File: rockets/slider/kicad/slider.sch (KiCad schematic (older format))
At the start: 34 parts

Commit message: More shematic
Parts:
- added J?: SWD Breakout, symbol Connector:Conn_01x03_Male
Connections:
- net Buzzer_EN: now also U?.19 (GPIO14)
- net GND: now also J?.2 (Pin_2)
- net PWM_Buzzer: now also U?.17 (GPIO13)
- net SWD_CLK: now reaches U?.41 (SWCLK)
- net SWD_CLK: now also J?.3 (Pin_3)
- net SWD_IO: now reaches U?.43 (SWDIO)
- net SWD_IO: now also J?.1 (Pin_1)
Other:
- moved on the sheet: BT?, BZ?, C?, D?, J?, LS?, M?, Q?, R?, SW?, U?

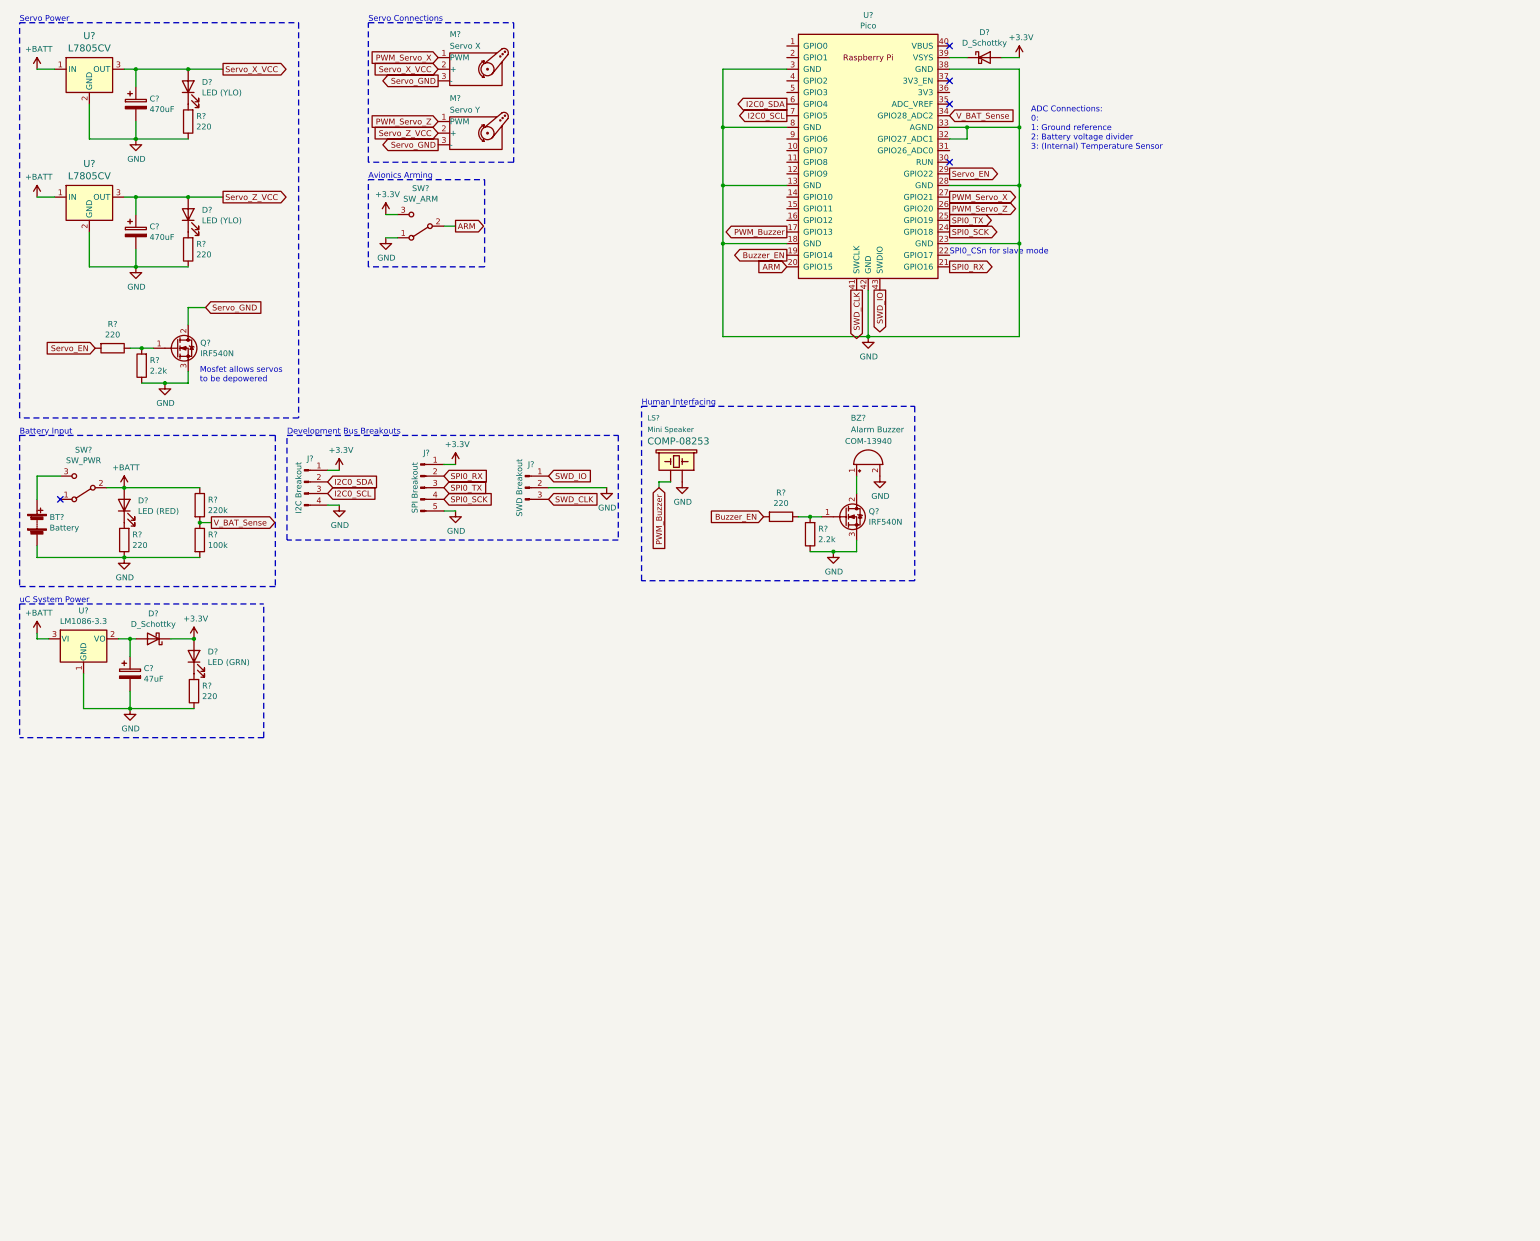
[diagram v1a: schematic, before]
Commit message: Change schematic layout
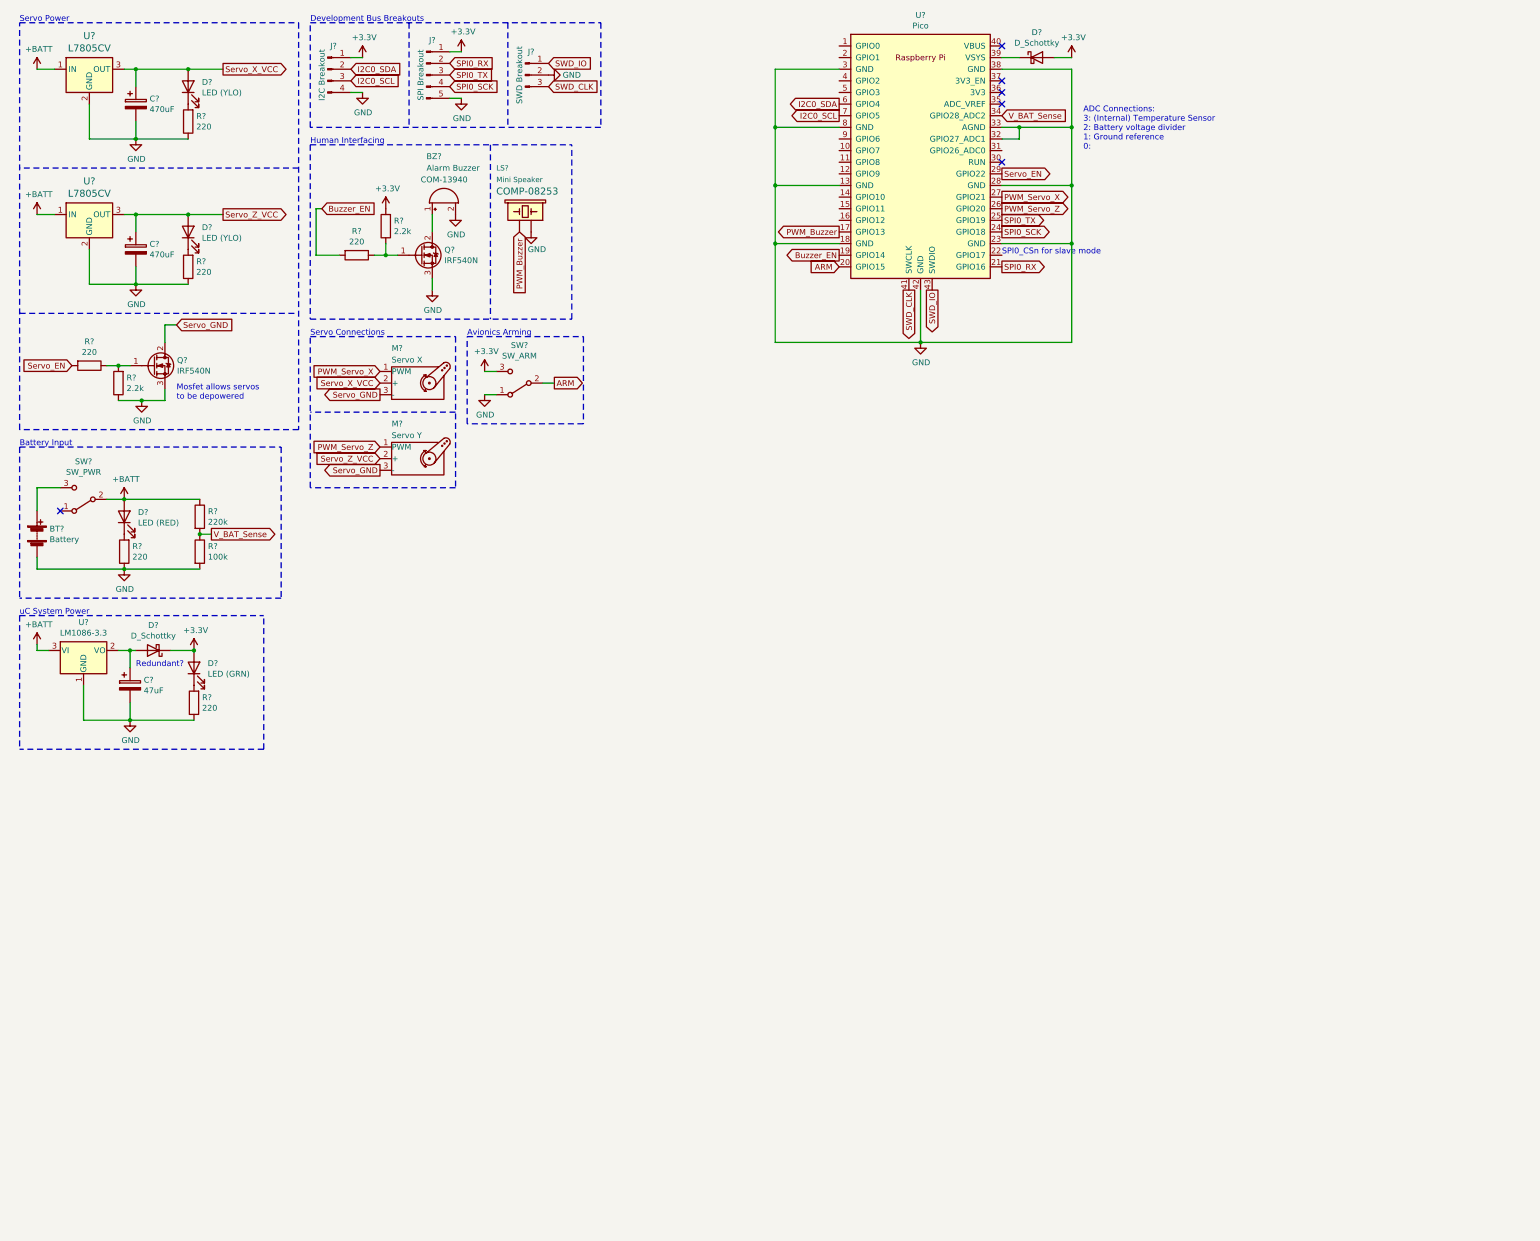
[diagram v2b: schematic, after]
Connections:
- net +3V3: now also R?.2
- net GND: no longer R?.1
- net at Q?.1 (G), R?.1: now also R?.1; no longer R?.2
- no-connect marks 5 -> 6
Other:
- note added: "ADC Connections:\n3: (Internal) Temperature Sensor\n2: Battery voltage divider\n1: Ground reference\n0:"
- note added: "Redundant?"
- note removed: "ADC Connections:\n0:\n1: Ground reference\n2: Battery voltage divider\n3: (Internal) Temperature Sensor"
- moved on the sheet: BT?, BZ?, C?, D?, J?, LS?, M?, Q?, R?, SW?, U?

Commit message: layouting
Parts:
- removed D?: D_Schottky, symbol Device:D_Schottky
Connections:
- net +3V3: now also C?.1, U?.2 (VO)
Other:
- note added: "L7805CV\nMin: +2v = 7v\nMax: 35v"
- note added: "LM1086-3.3\nMin: +1.5v = 4.8v\nMax: +27v = 30.3v"
- note added: "Min: 7v (L785CV)\nMax: 30.3v (LM1086-3.3)"
- note removed: "Redundant?"
- moved on the sheet: BT?, C?, D?, R?, SW?, U?

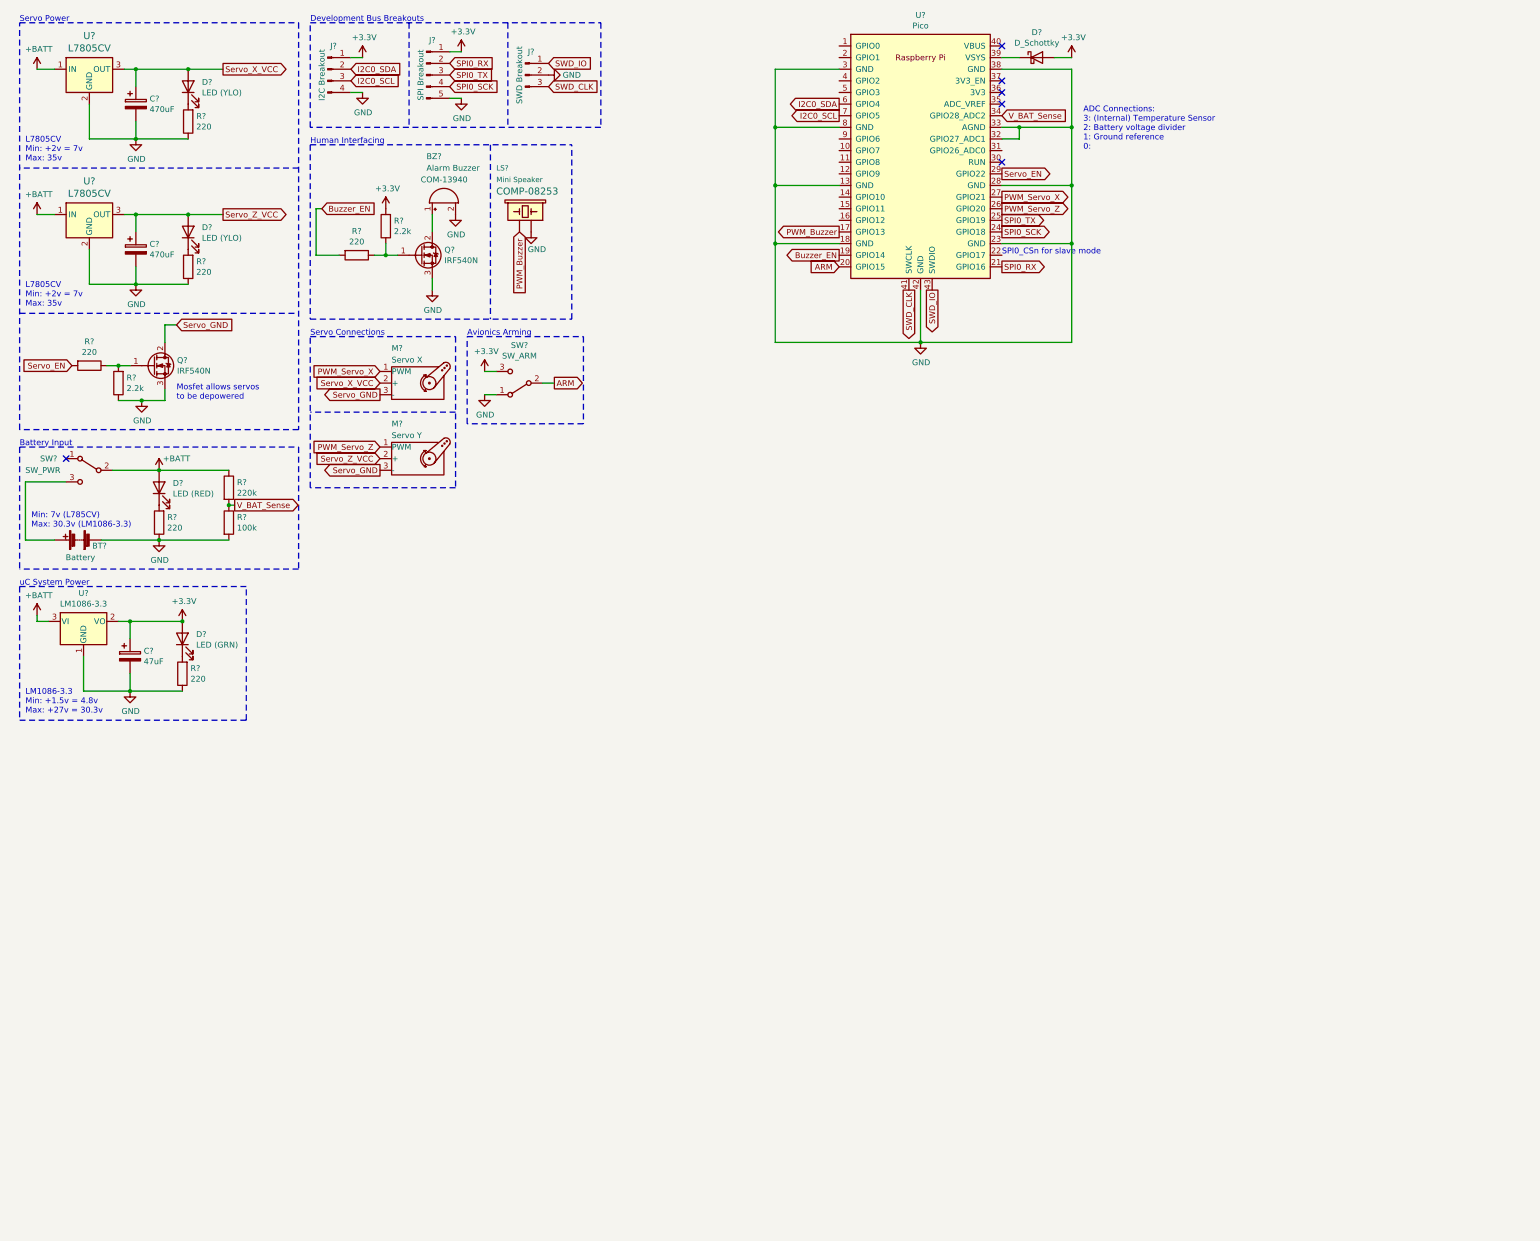
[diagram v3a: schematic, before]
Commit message: assigned footprints
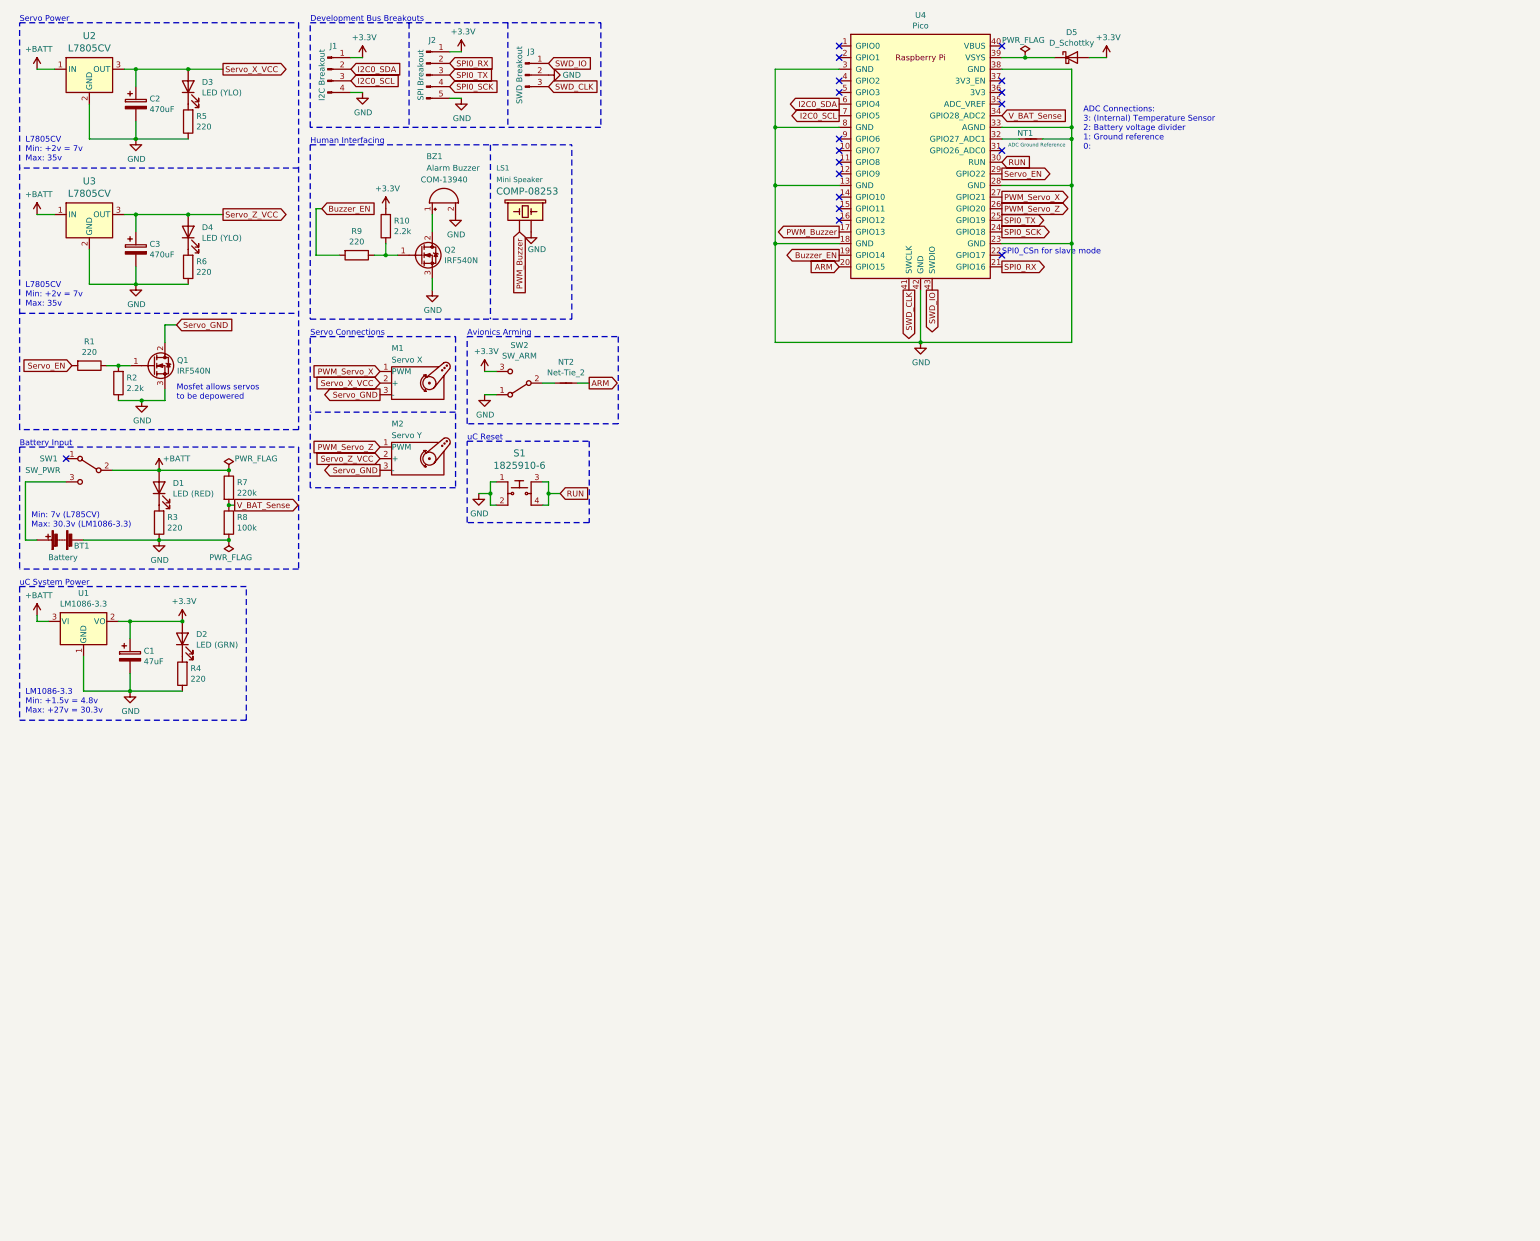
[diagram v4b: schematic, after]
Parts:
- added NT1: ADC Ground Reference, NetTie:NetTie-2_SMD_Pad2.0mm, symbol Device:Net-Tie_2
- added NT2: Net-Tie_2, NetTie:NetTie-2_SMD_Pad2.0mm, symbol Device:Net-Tie_2
- added S1: 1825910-6, digikey-footprints:Switch_Tactile_THT_6x6mm, symbol dk_Tactile-Switches:1825910-6
- D1, D2, D3, D4: renamed from D?; footprint (none) -> LED_THT:LED_D5.0mm
- D5: renamed from D?; footprint (none) -> Diode_THT:D_DO-35_SOD27_P10.16mm_Horizontal
- J1: renamed from J?; footprint (none) -> Connector_PinHeader_2.54mm:PinHeader_1x04_P2.54mm_Vertical
- J2: renamed from J?; footprint (none) -> Connector_PinHeader_2.54mm:PinHeader_1x05_P2.54mm_Vertical
- J3: renamed from J?; footprint (none) -> Connector_PinHeader_2.54mm:PinHeader_1x03_P2.54mm_Vertical
- LS1: renamed from LS?; footprint BUZZER-12MM -> Sparkfun Electromechanical:BUZZER-12MM
- M1, M2: renamed from M?; footprint (none) -> Connector_PinHeader_2.54mm:PinHeader_1x03_P2.54mm_Vertical
- R1, R10, R2, R3, R4, R5, R6, R7, R8, R9: renamed from R?; footprint (none) -> Resistor_THT:R_Axial_DIN0207_L6.3mm_D2.5mm_P7.62mm_Horizontal
- U1: renamed from U?; footprint (none) -> Package_TO_SOT_THT:TO-220-3_Vertical
- U2, U3: renamed from U?; footprint digikey-footprints:TO-220-3 -> Package_TO_SOT_THT:TO-220-3_Vertical
- gave numbers to parts that had none: 10
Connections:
- net ARM: now also NT2.2; no longer SW2.2 (B)
- net GND: now also NT1.1, S1.1, S1.2; no longer U4.32 (GPIO27_ADC1)
- net RUN: now reaches U4.30 (RUN)
- net RUN: now also S1.3, S1.4
- new net: NT1.2, U4.32 (GPIO27_ADC1)
- new net: NT2.1, SW2.2 (B)
- no-connect marks 6 -> 18
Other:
- note added: "uC Reset"
- moved on the sheet: BT1, D5

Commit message: pcb
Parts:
- added J4: Pyro 1 Terminal, TerminalBlock_4Ucon:TerminalBlock_4Ucon_1x02_P3.50mm_Horizontal, symbol Connector:Screw_Terminal_01x02
- added Q3: IRF540N, Package_TO_SOT_THT:TO-220-3_Vertical, symbol Transistor_FET:IRF540N
- added R11: 220, Resistor_THT:R_Axial_DIN0207_L6.3mm_D2.5mm_P7.62mm_Horizontal, symbol Device:R
- added R12: 2.2k, Resistor_THT:R_Axial_DIN0207_L6.3mm_D2.5mm_P7.62mm_Horizontal, symbol Device:R
- added R13: 220k, Resistor_THT:R_Axial_DIN0207_L6.3mm_D2.5mm_P7.62mm_Horizontal, symbol Device:R
- added R14: 100k, Resistor_THT:R_Axial_DIN0207_L6.3mm_D2.5mm_P7.62mm_Horizontal, symbol Device:R
- BT1: footprint (none) -> TerminalBlock_4Ucon:TerminalBlock_4Ucon_1x02_P3.50mm_Horizontal
- BZ1: footprint (none) -> slider:CE-C75-Piezo-Alarm
- C1: footprint (none) -> Capacitor_THT:CP_Radial_D5.0mm_P2.50mm
- C2, C3: footprint (none) -> Capacitor_THT:CP_Radial_D10.0mm_P2.50mm
- NT1, NT2: footprint NetTie:NetTie-2_SMD_Pad2.0mm -> NetTie:NetTie-2_SMD_Pad0.5mm
- SW1, SW2: footprint (none) -> Connector_PinHeader_2.54mm:PinHeader_1x03_P2.54mm_Vertical
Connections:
- net +3V3: now also J1.4 (Pin_4), J2.5 (Pin_5); no longer J1.1 (Pin_1), J2.1 (Pin_1)
- net +BATT: now also J4.2 (Pin_2)
- net GND: now also J1.1 (Pin_1), J2.1 (Pin_1), Q3.3 (S), R12.1, R14.2; no longer J1.4 (Pin_4), J2.5 (Pin_5)
- net I2C0_SCL: now also J1.2 (Pin_2); no longer J1.3 (Pin_3)
- net I2C0_SDA: now also J1.3 (Pin_3); no longer J1.2 (Pin_2)
- net SPI0_RX: now also J2.4 (Pin_4); no longer J2.2 (Pin_2)
- net SPI0_SCK: now also J2.2 (Pin_2); no longer J2.4 (Pin_4)
- net Pyro_1: now reaches U4.14 (GPIO10)
- net Pyro_1: now also R11.2
- net Pyro_1_Cont: now reaches U4.15 (GPIO11)
- net Pyro_1_Cont: now also R13.2, R14.1
- net Buzzer_EN renamed Alarm_EN
- new net: Q3.1 (G), R11.1, R12.2
- new net: J4.1 (Pin_1), Q3.2 (D), R13.1
- no-connect marks 18 -> 16
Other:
- note added: "Pyro Channels"
- note added: "Subject to change\nTODO:"
- note added: "UUH, maybe some\ncurrent limiting?"

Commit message: loads of pcb shiz
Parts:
- removed D2: LED (GRN), LED_THT:LED_D5.0mm, symbol Device:LED
- removed D3, D4: LED (YLO), LED_THT:LED_D5.0mm, symbol Device:LED
- removed J3: SWD Breakout, Connector_PinHeader_2.54mm:PinHeader_1x03_P2.54mm_Vertical, symbol Connector:Conn_01x03_Male
- removed NT2: Net-Tie_2, NetTie:NetTie-2_SMD_Pad0.5mm, symbol Device:Net-Tie_2
- removed R4, R5, R6: 220, Resistor_THT:R_Axial_DIN0207_L6.3mm_D2.5mm_P7.62mm_Horizontal, symbol Device:R
- removed SW1: SW_PWR, Connector_PinHeader_2.54mm:PinHeader_1x03_P2.54mm_Vertical, symbol Switch:SW_SPDT
- added H1, H2: MountingHole, MountingHole:MountingHole_3mm, symbol Mechanical:MountingHole
- added SW?: SW_SPDT, symbol Switch:SW_SPDT
- BT1: footprint TerminalBlock_4Ucon:TerminalBlock_4Ucon_1x02_P3.50mm_Horizontal -> TerminalBlock_Phoenix:TerminalBlock_Phoenix_PT-1,5-2-3.5-H_1x02_P3.50mm_Horizontal
- C2, C3: value 470uF -> 100uF; footprint Capacitor_THT:CP_Radial_D10.0mm_P2.50mm -> Capacitor_THT:CP_Radial_D6.3mm_P2.50mm
- D5: footprint Diode_THT:D_DO-35_SOD27_P10.16mm_Horizontal -> Diode_THT:D_DO-35_SOD27_P7.62mm_Horizontal
- SW2: value SW_ARM -> SW_SPDT; footprint Connector_PinHeader_2.54mm:PinHeader_1x03_P2.54mm_Vertical -> (none)
- U4: footprint RPi_Pico:RPi_Pico_SMD_TH -> RPi_Pico:RPi_Pico_TH_Perfboard; symbol MCU_RaspberryPi_and_Boards:Pico -> MCU_RaspberryPi_and_Boards:Pico_PerfBoard
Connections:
- net +3V3: now also SW?.3 (C); no longer SW2.3 (C)
- net +BATT: now also SW2.1 (A)
- net ARM: now also SW?.2 (B)
- net GND: now also SW?.1 (A); no longer SW2.1 (A), U4.42 (GND)
- net at BT1.1 (+): now also SW2.2 (B)
- removed net SWD_CLK: U4.41 (SWCLK)
- removed net SWD_IO: U4.43 (SWDIO)
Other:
- note added: "Arming Switch"
- note removed: "Avionics Arming"
